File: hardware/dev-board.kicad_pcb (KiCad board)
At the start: 2 copper layers, 46 x 23.1 mm, 4 parts, among them J1 Conn_Chameleon_SWD, J3 Conn_01x18_Male, J4 Conn_01x18_Male, U1 E73-2G4M08S1C

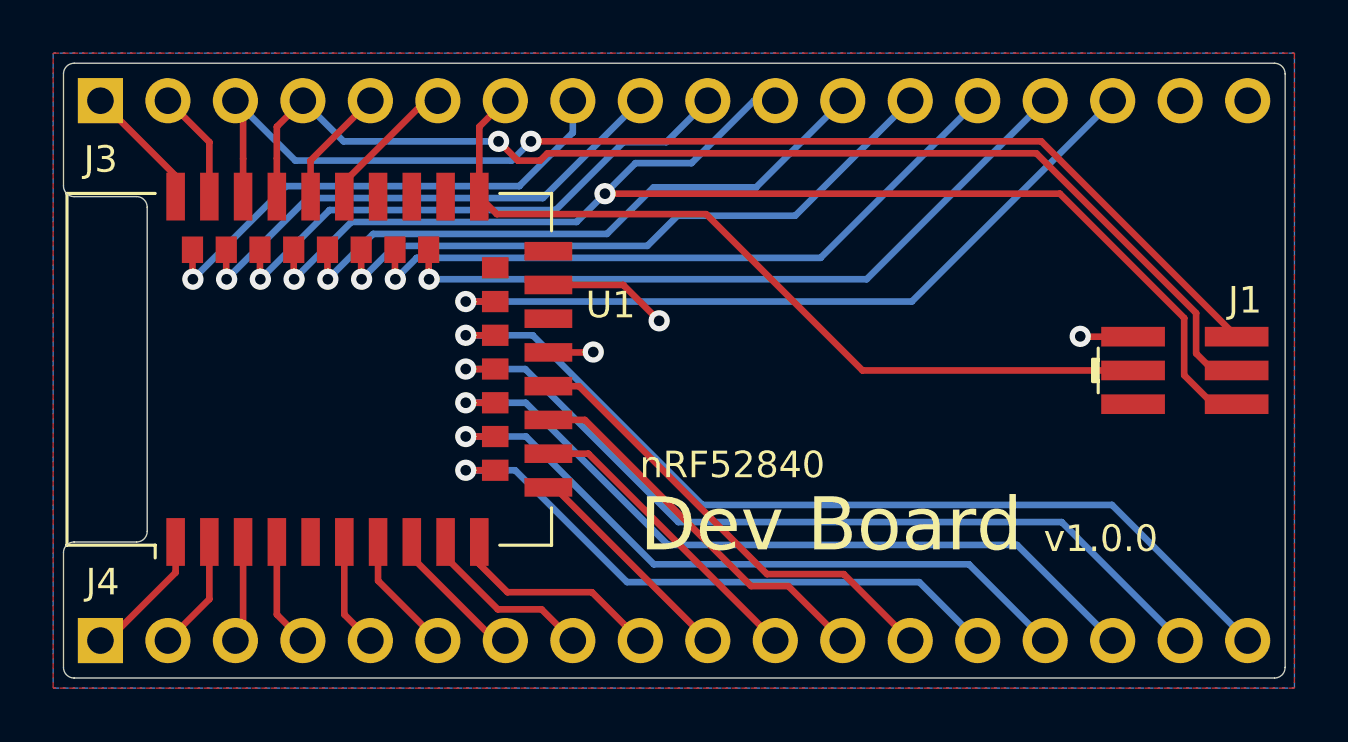
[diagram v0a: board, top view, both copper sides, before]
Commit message: nrf52820 schematic
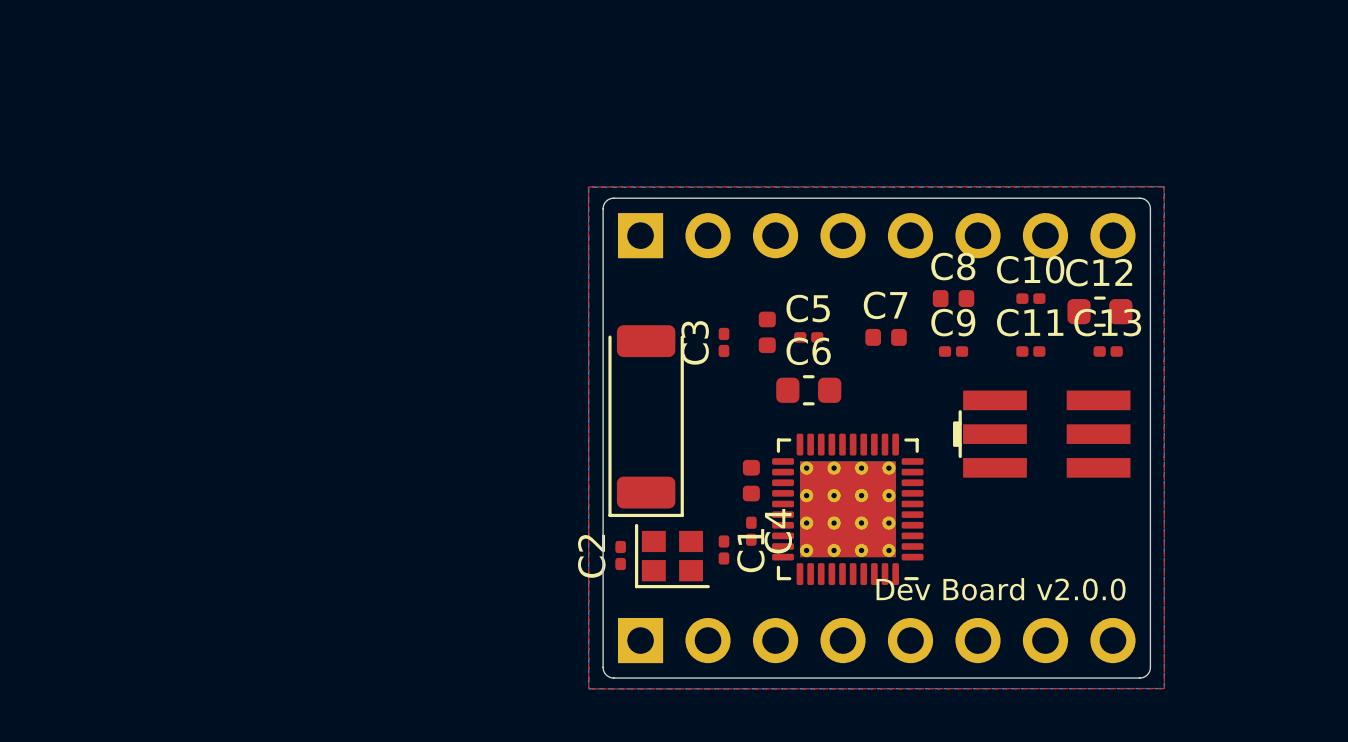
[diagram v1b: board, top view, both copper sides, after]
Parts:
- removed J4: Conn_01x18_Male, Connector_PinHeader_2.54mm:PinHeader_1x18_P2.54mm_Vertical
- added AE1: Antenna_Chip, RF_Antenna:Johanson_2450AT43F0100, F.Cu at (144.4, 100.3)
- added C1: 15p, Capacitor_SMD:C_0201_0603Metric, F.Cu at (147.4, 105.4)
- added C10: 100p, Capacitor_SMD:C_0201_0603Metric, F.Cu at (158.9, 95.9)
- added C11: 820p, Capacitor_SMD:C_0201_0603Metric, F.Cu at (158.9, 97.9)
- added C12: 4.7u, Capacitor_SMD:C_0603_1608Metric, F.Cu at (161.5, 96.4)
- added C13: 100n, Capacitor_SMD:C_0201_0603Metric, F.Cu at (161.8, 97.9)
- added C2: 15p, Capacitor_SMD:C_0201_0603Metric, F.Cu at (143.5, 105.6)
- added C3: 1p, Capacitor_SMD:C_0201_0603Metric, F.Cu at (147.4, 97.5)
- added C4: 1p, Capacitor_SMD:C_0201_0603Metric, F.Cu at (148.4, 104.7)
- added C5: 100n, Capacitor_SMD:C_0201_0603Metric, F.Cu at (150.6, 97.4)
- added C6: 1u, Capacitor_SMD:C_0603_1608Metric, F.Cu at (150.6, 99.3)
- added C7: 1u, Capacitor_SMD:C_0402_1005Metric, F.Cu at (153.5, 97.4)
- added C8: 1u, Capacitor_SMD:C_0402_1005Metric, F.Cu at (156.0, 95.9)
- added C9: 100n, Capacitor_SMD:C_0201_0603Metric, F.Cu at (156.0, 97.9)
- added J2: Conn_01x08, Connector_PinHeader_2.54mm:PinHeader_1x08_P2.54mm_Vertical, B.Cu at (144.2, 108.8)
- added L1: 2.2n, Inductor_SMD:L_0402_1005Metric, F.Cu at (149.0, 97.2)
- added L2: 4.7n, Inductor_SMD:L_0402_1005Metric, F.Cu at (148.4, 102.8)
- added Y1: Crystal_GND24, Crystal:Crystal_SMD_2016-4Pin_2.0x1.6mm, F.Cu at (145.4, 105.6)
- J3: value Conn_01x18_Male -> Conn_01x08; footprint Connector_PinHeader_2.54mm:PinHeader_1x18_P2.54mm_Vertical -> Connector_PinHeader_2.54mm:PinHeader_1x08_P2.54mm_Vertical
- U1: value E73-2G4M08S1C -> nRF52820-QDxx; footprint IoT_Home:E73-2G4M08S1C -> Package_DFN_QFN:QFN-40-1EP_5x5mm_P0.4mm_EP3.6x3.6mm_ThermalVias
- moved J3 21.0 mm to (144.2, 93.5)
- moved U1 20.9 mm to (152.0, 103.8), turned to 180 degrees
- moved J1 5.72 mm to (159.5, 101.0)
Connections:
- J1 pad 2: /SWDCLK -> GND
- J1 pad 3: /P0.18 -> /RX
- J1 pad 5: GND -> /TX
- J1 pad 6: /SWO -> /SWDCLK
- J3 pad 1: /P0.10 -> /P0.16
- J3 pad 2: /P0.09 -> /P0.14
- J3 pad 3: /SWDCLK -> /P0.04
- J3 pad 4: /SWDIO -> /P0.08
- J3 pad 5: /P0.24 -> /P0.06
- J3 pad 6: /P0.13 -> /P0.20
- J3 pad 7: /P0.18 -> /P0.17
- J3 pad 8: /P1.06 -> /P0.05
- U1 pad 1: /P1.11 -> +3V3
- U1 pad 10: /P0.30 -> GND
- U1 pad 11: /P0.00 -> (no net)
- U1 pad 12: /P0.26 -> (no net)
- U1 pad 13: /P0.11 -> (no net)
- U1 pad 14: /P0.06 -> /P0.14
- U1 pad 15: /P0.05 -> /P0.15
- U1 pad 16: /P0.08 -> /P0.18
- U1 pad 17: /P1.09 -> /P0.20
- U1 pad 18: /P0.04 -> +3V3
- U1 pad 19: +3V3 -> /SWDIO
- U1 pad 2: /P1.10 -> (no net)
- U1 pad 20: /P0.12 -> /SWDCLK
- U1 pad 21: GND -> +3V3
- U1 pad 22: /P0.07 -> /P0.16
- U1 pad 23: +3V3 -> /P0.17
- U1 pad 24: GND -> Net-(C4-Pad1)
- U1 pad 25: (no net) -> GND
- U1 pad 26: /P0.18 -> +3V3
- U1 pad 27: (no net) -> +3V3
- U1 pad 28: /P0.15 -> Net-(C1-Pad1)
- U1 pad 29: (no net) -> Net-(C2-Pad1)
- U1 pad 3: /P0.03 -> (no net)
- U1 pad 30: /P0.17 -> +3V3
- U1 pad 31: (no net) -> /P0.08
- U1 pad 32: /P0.20 -> /RX
- U1 pad 33: /P0.13 -> /TX
- U1 pad 34: /P0.22 -> /P0.28
- U1 pad 35: /P0.24 -> /P0.03
- U1 pad 36: /SWO -> /P0.02
- U1 pad 37: /SWDIO -> GND
- U1 pad 38: /P1.02 -> +3V3
- U1 pad 39: /SWDCLK -> (no net)
- U1 pad 4: /P0.28 -> /P0.04
- U1 pad 40: /P1.04 -> GND
- U1 pad 41: /P0.09 -> GND
- U1 pad 5: GND -> /P0.05
- U1 pad 6: /P1.13 -> /P0.06
- U1 pad 7: /P0.02 -> /P0.07
- U1 pad 8: /P0.29 -> +3V3
- U1 pad 9: /P0.31 -> +3V3
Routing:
- net /SWO: track 50.3 -> 0.00 mm, vias 2 -> 0
- net /SWDCLK: track 45.7 -> 0.00 mm, vias 1 -> 0
- net /SWDIO: track 44.5 -> 0.00 mm, vias 1 -> 0
- net /P0.12: track 35.3 -> 0.00 mm, vias 1 -> 0
- net /P0.04: track 32.2 -> 0.00 mm, vias 1 -> 0
- net /P0.18: track 31.3 -> 0.00 mm
- net /P0.08: track 29.2 -> 0.00 mm, vias 1 -> 0
- net /P0.07: track 28.6 -> 0.00 mm, vias 1 -> 0
- net /P0.15: track 27.1 -> 0.00 mm, vias 1 -> 0
- net /P0.06: track 26.1 -> 0.00 mm, vias 1 -> 0
- net /P0.17: track 25.8 -> 0.00 mm, vias 1 -> 0
- net /P0.20: track 24.5 -> 0.00 mm, vias 1 -> 0
- net /P0.22: track 23.3 -> 0.00 mm, vias 1 -> 0
- net /P0.26: track 23.0 -> 0.00 mm, vias 1 -> 0
- net /P1.02: track 20.7 -> 0.00 mm, vias 1 -> 0
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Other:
- board size 46 x 23.1 mm -> 20.6 x 18.1 mm
- copper layers 2 -> 4
- net class Default: clearance 0.2 -> 0.09; trace_width 0.25 -> 0.09
- rule pad_to_mask_clearance: 0.051 -> 0
- rule trace_clearance: 0.2 -> 0.09
- rule trace_min: 0.127 -> 0.09
- board text added: "Dev Board v2.0.0"
- board text removed: "0.00"
- board text removed: "0.02"
- board text removed: "0.04"
- board text removed: "0.05"
- board text removed: "0.09"
- board text removed: "0.10"
- board text removed: "0.11"
- board text removed: "0.12"
- board text removed: "0.13"
- board text removed: "0.18"
- board text removed: "0.24"
- board text removed: "0.28"
- board text removed: "0.29"
- board text removed: "0.30"
- board text removed: "0.31"
- board text removed: "1.06"
- board text removed: "1.10"
- board text removed: "1.11"
- board text removed: "1.13"
- board text removed: "3V3"
- board text removed: "Dev Board"
- board text removed: "GND"
- board text removed: "SWCLK"
- board text removed: "SWDIO"
- board text removed: "nRF52840"
- board text removed: "v1.0.0"
